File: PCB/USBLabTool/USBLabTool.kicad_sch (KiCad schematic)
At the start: 0 parts

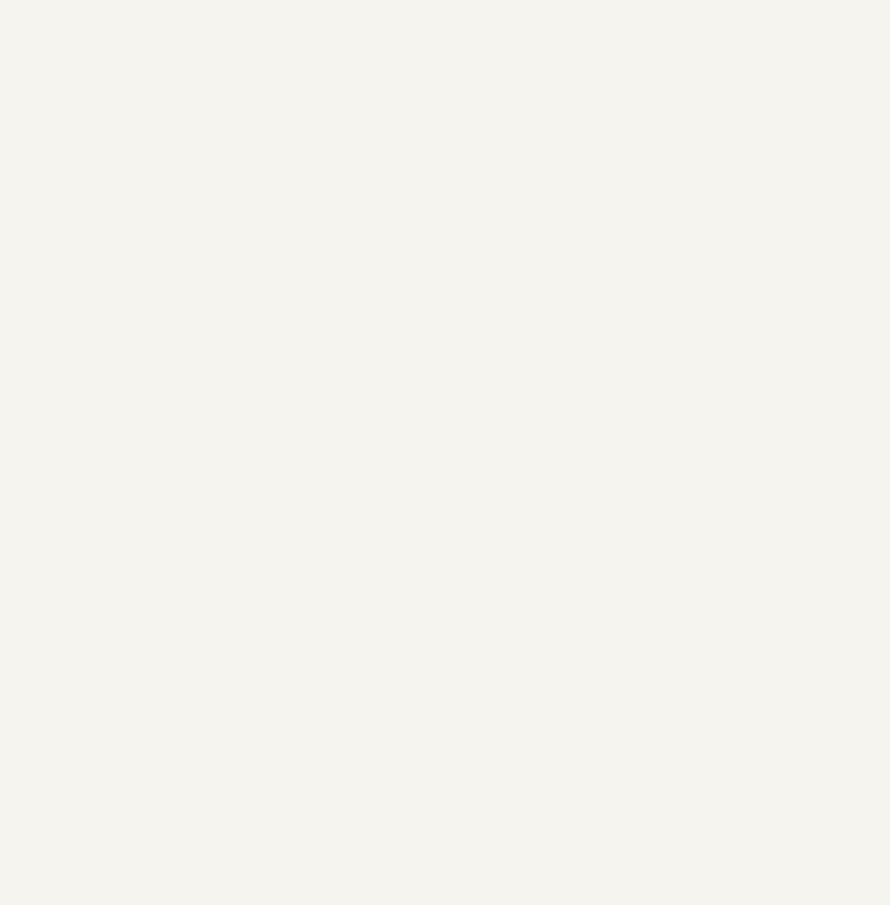
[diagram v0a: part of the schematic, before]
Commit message: change USB design and MCU
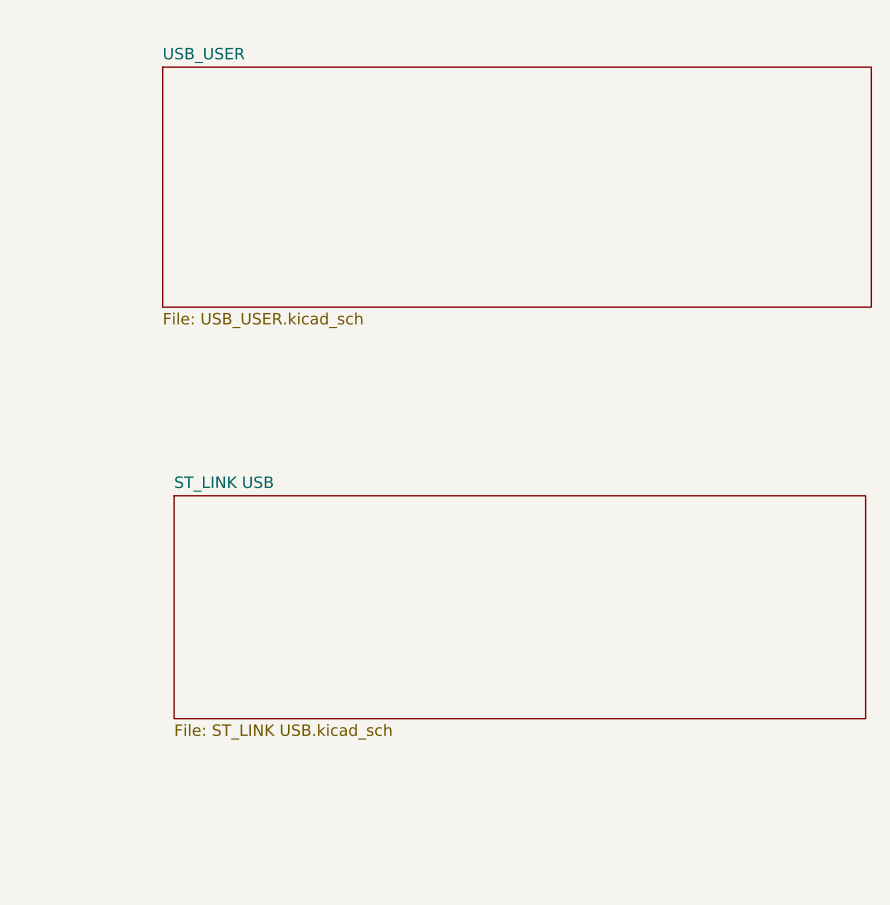
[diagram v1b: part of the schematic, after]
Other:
- added sheet ST_LINK USB (ST_LINK USB.kicad_sch)
- added sheet USB_USER (USB_USER.kicad_sch)
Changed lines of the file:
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@@
+	)
+	(sheet
+		(at 297.18 36.83)
+		(size 78.74 26.67)
+		(fields_autoplaced yes)
+		(stroke
+			(width 0.1524)
+			(type solid)
+		)
+		(fill
+			(color 0 0 0 0.0000)
+		)
+		(property "Sheetname" "USB_USER"
+			(at 297.18 36.1184 0)
+			(effects
+				(font
+					(size 1.27 1.27)
+				)
+				(justify left bottom)
+			)
+		)
+		(property "Sheetfile" "USB_USER.kicad_sch"
+			(at 297.18 64.0846 0)
+			(effects
+				(font
+					(size 1.27 1.27)
+				)
+				(justify left top)
+			)
+		)
+		(instances
+			(project "USBLabTool"
+				(path "/b5440f7d-90d5-417e-adc2-aa6b11e5424d"
+					(page "6")
+				)
+			)
+		)
 	)
 	(sheet
@@
 				)
 			)
+		)
+	)
+	(sheet
+		(at 298.45 84.455)
+		(size 76.835 24.765)
+		(fields_autoplaced yes)
+		(stroke
+			(width 0.1524)
+			(type solid)
+		)
+		(fill
+			(color 0 0 0 0.0000)
+		)
+		(property "Sheetname" "ST_LINK USB"
+			(at 298.45 83.7434 0)
+			(effects
+				(font
+					(size 1.27 1.27)
+				)
+				(justify left bottom)
+			)
+		)
+		(property "Sheetfile" "ST_LINK USB.kicad_sch"
+			(at 298.45 109.8046 0)
+			(effects
+				(font
+					(size 1.27 1.27)
+				)
+				(justify left top)
+			)
+		)
+		(instances
+			(project "USBLabTool"
+				(path "/b5440f7d-90d5-417e-adc2-aa6b11e5424d"
+					(page "7")
+				)
+			)
